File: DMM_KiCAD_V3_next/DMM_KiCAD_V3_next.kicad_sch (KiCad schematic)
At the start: 69 parts, among them J1 Conn_01x07_Pin, J10 ANALOG, J11 I_Input, J12 Conn_01x02_Pin, J13 DIGITAL1, J14 Barrel_Jack, J15 Barrel_Jack, J2 MicoSD, J3 Conn_01x07_Pin, J31 Conn_01x04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

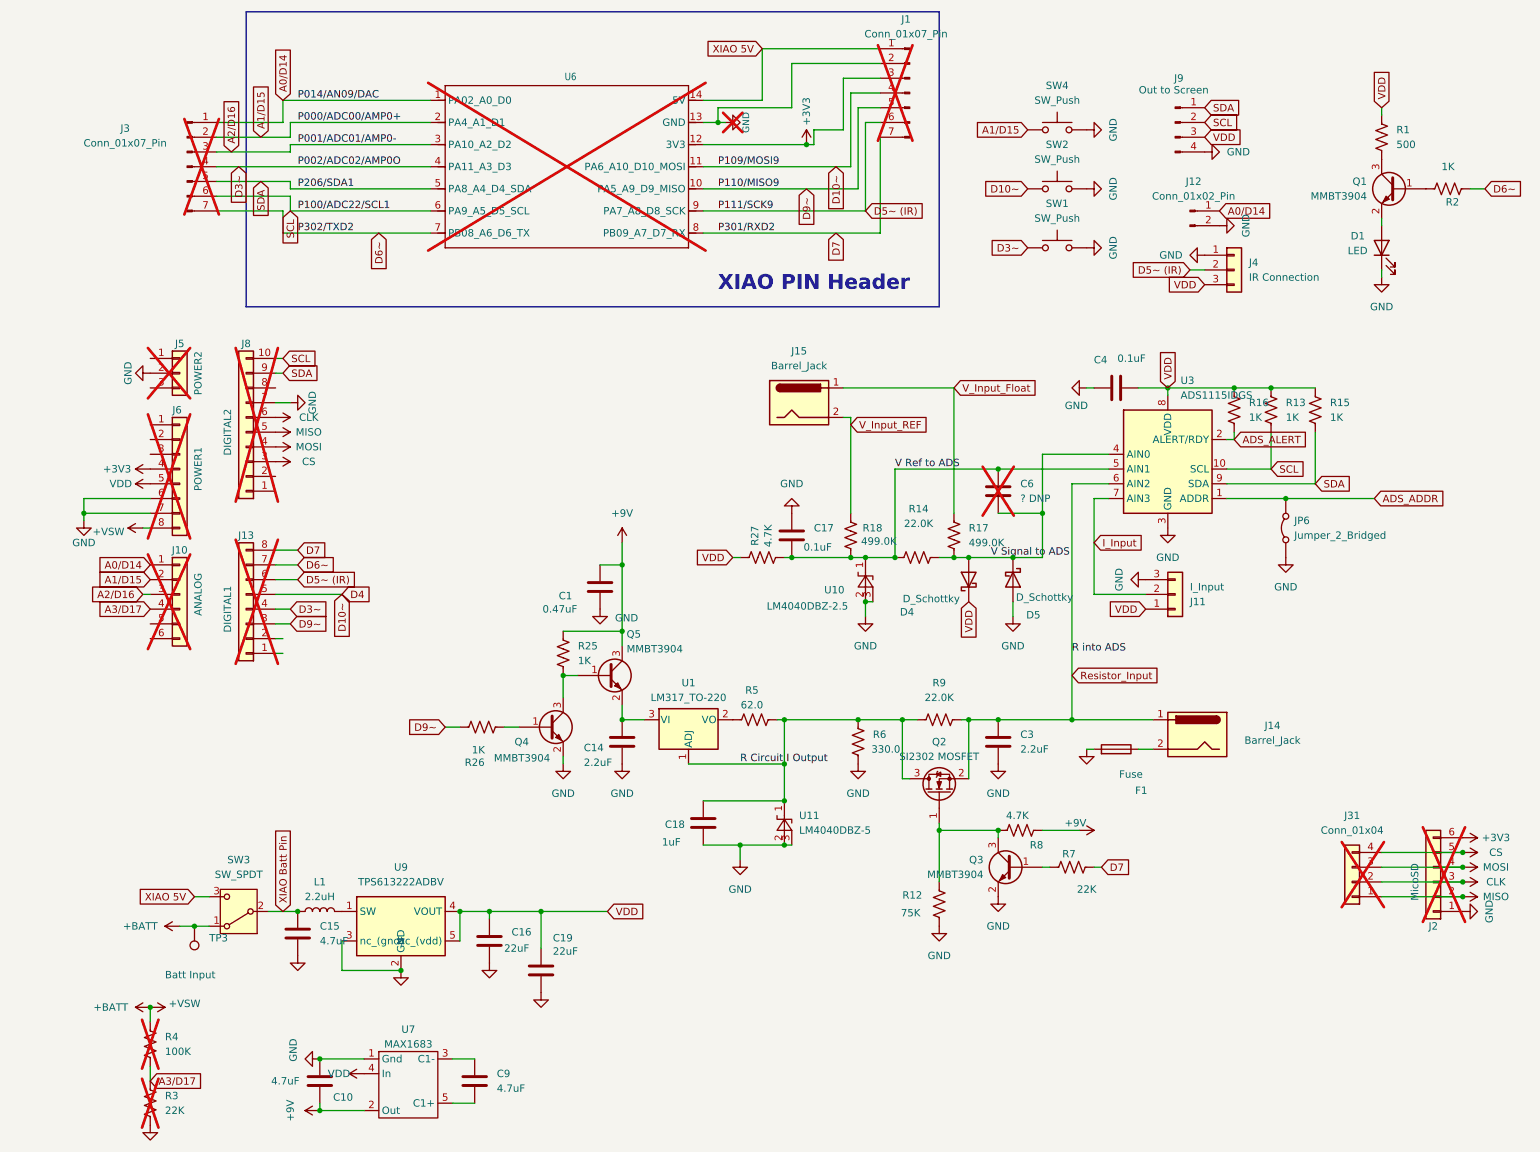
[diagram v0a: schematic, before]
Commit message: Working on a Giga-COmpatible DMM code.
Also working on adding level shifting to the next PCB design.
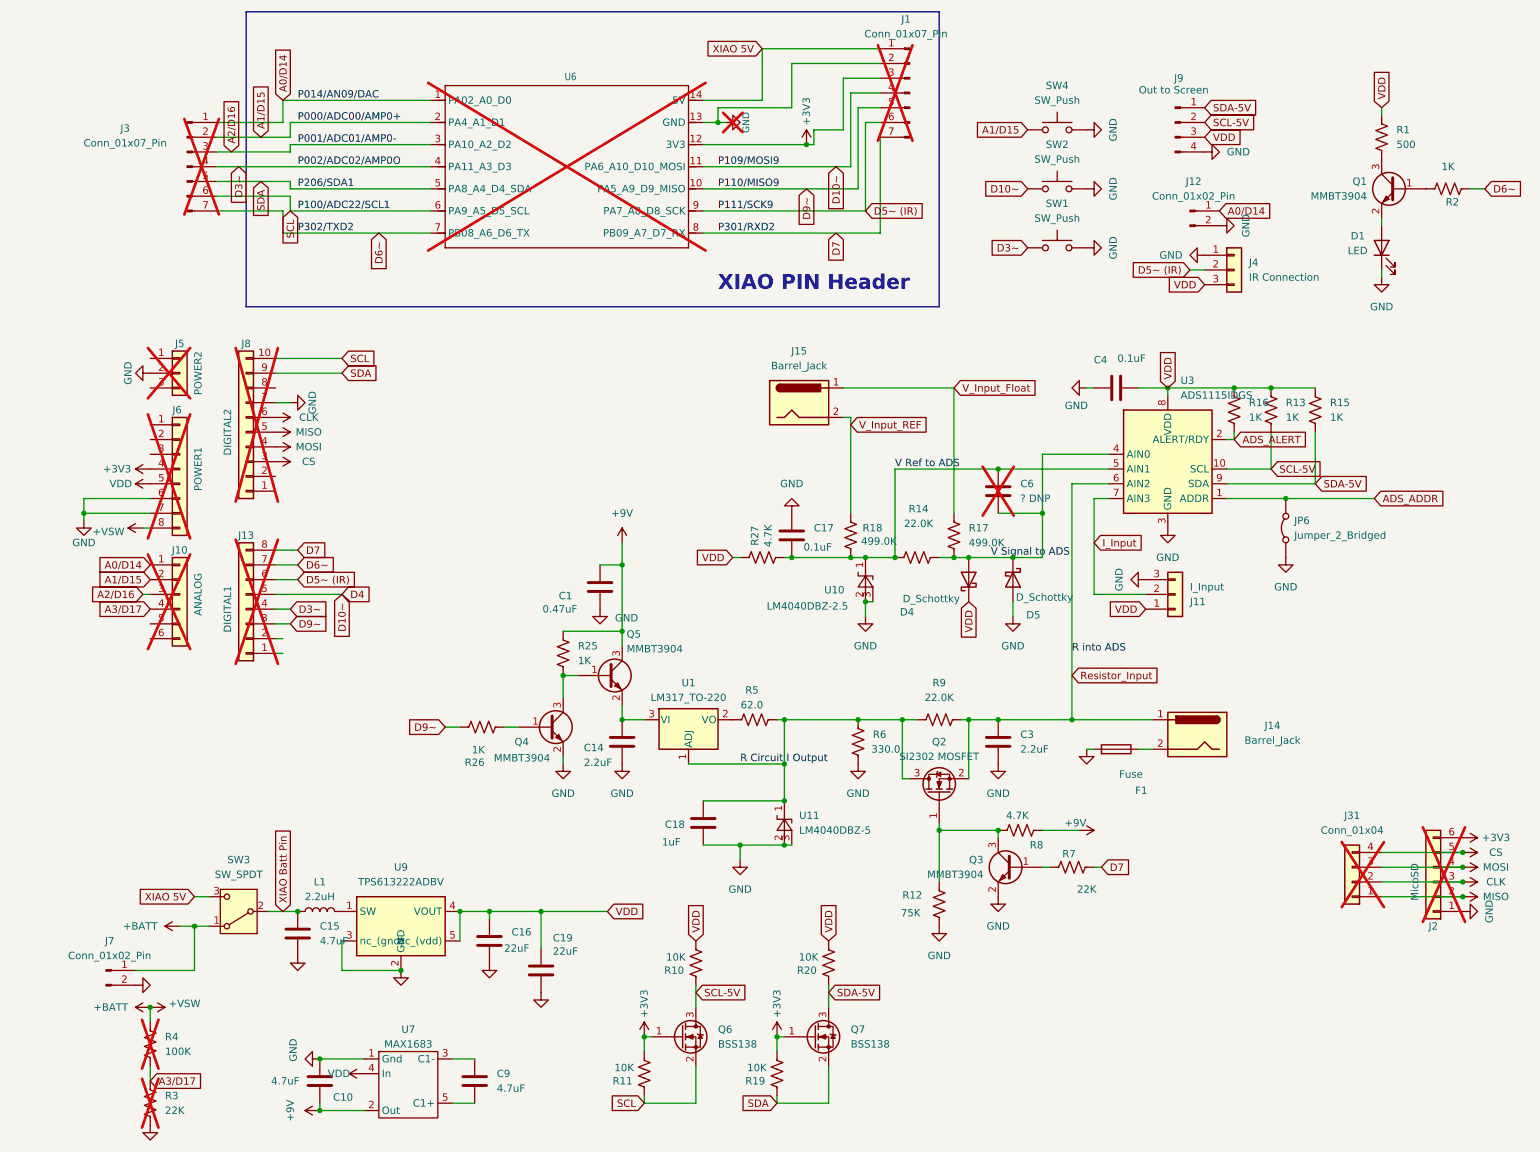
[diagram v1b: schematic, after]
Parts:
- removed TP3: Batt Input, Connector_PinHeader_2.54mm:PinHeader_1x01_P2.54mm_Vertical, symbol Connector:TestPoint
- added J7: Conn_01x02_Pin, Connector_PinSocket_2.54mm:PinSocket_1x02_P2.54mm_Vertical, symbol Connector:Conn_01x02_Pin
- added Q6, Q7: BSS138, Package_TO_SOT_SMD:SOT-23, symbol Transistor_FET:BSS138
- added R10, R11, R19, R20: 10K, Resistor_SMD:R_0805_2012Metric_Pad1.20x1.40mm_HandSolder, symbol Device:R_US
- F1: footprint Fuse:Fuseholder_Clip-5x20mm_Keystone_3512P_Inline_P23.62x7.27mm_D1.02x2.41x1.02x1.57mm_Horizontal -> Fuse:Fuse_1206_3216Metric_Pad1.42x1.75mm_HandSolder
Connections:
- net +3V3: now also Q6.1 (G), Q7.1 (G), R11.2, R19.2
- net +BATT: now also J7.1 (Pin_1)
- net GND: now also J7.2 (Pin_2)
- net SCL: now also Q6.2 (S), R11.1; no longer J9.2 (Pin_2), R13.1, U3.10 (SCL)
- net SDA: now also Q7.2 (S), R19.1; no longer J9.1 (Pin_1), R15.1, U3.9 (SDA)
- net VDD: now also R10.2, R20.2
- new net SCL-5V: J9.2 (Pin_2), Q6.3 (D), R10.1, R13.1, U3.10 (SCL)
- new net SDA-5V: J9.1 (Pin_1), Q7.3 (D), R15.1, R20.1, U3.9 (SDA)

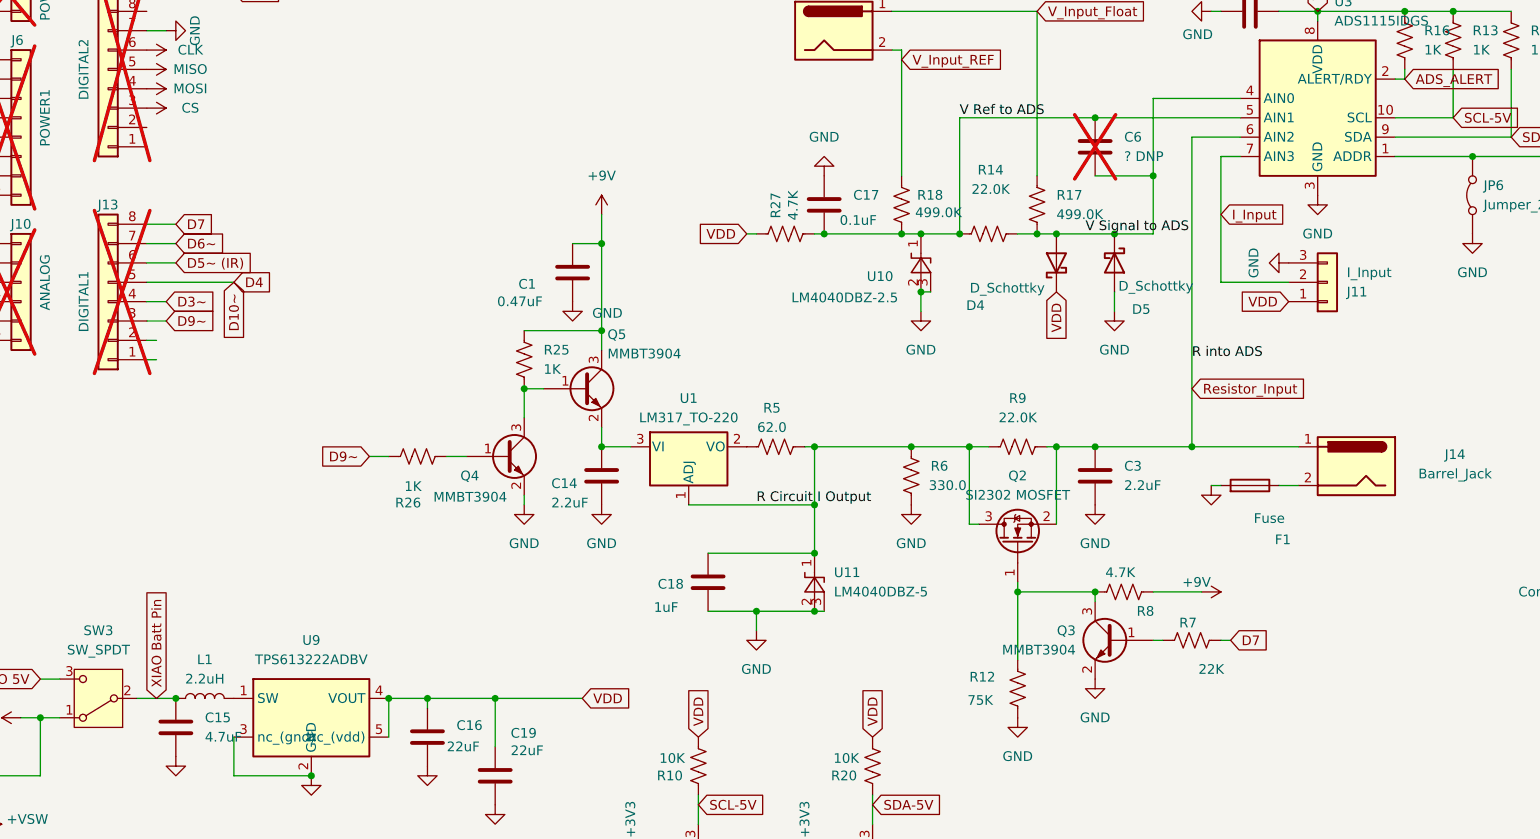
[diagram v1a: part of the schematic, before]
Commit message: PCB updates.
 Added the option for four-wire resistance measurements
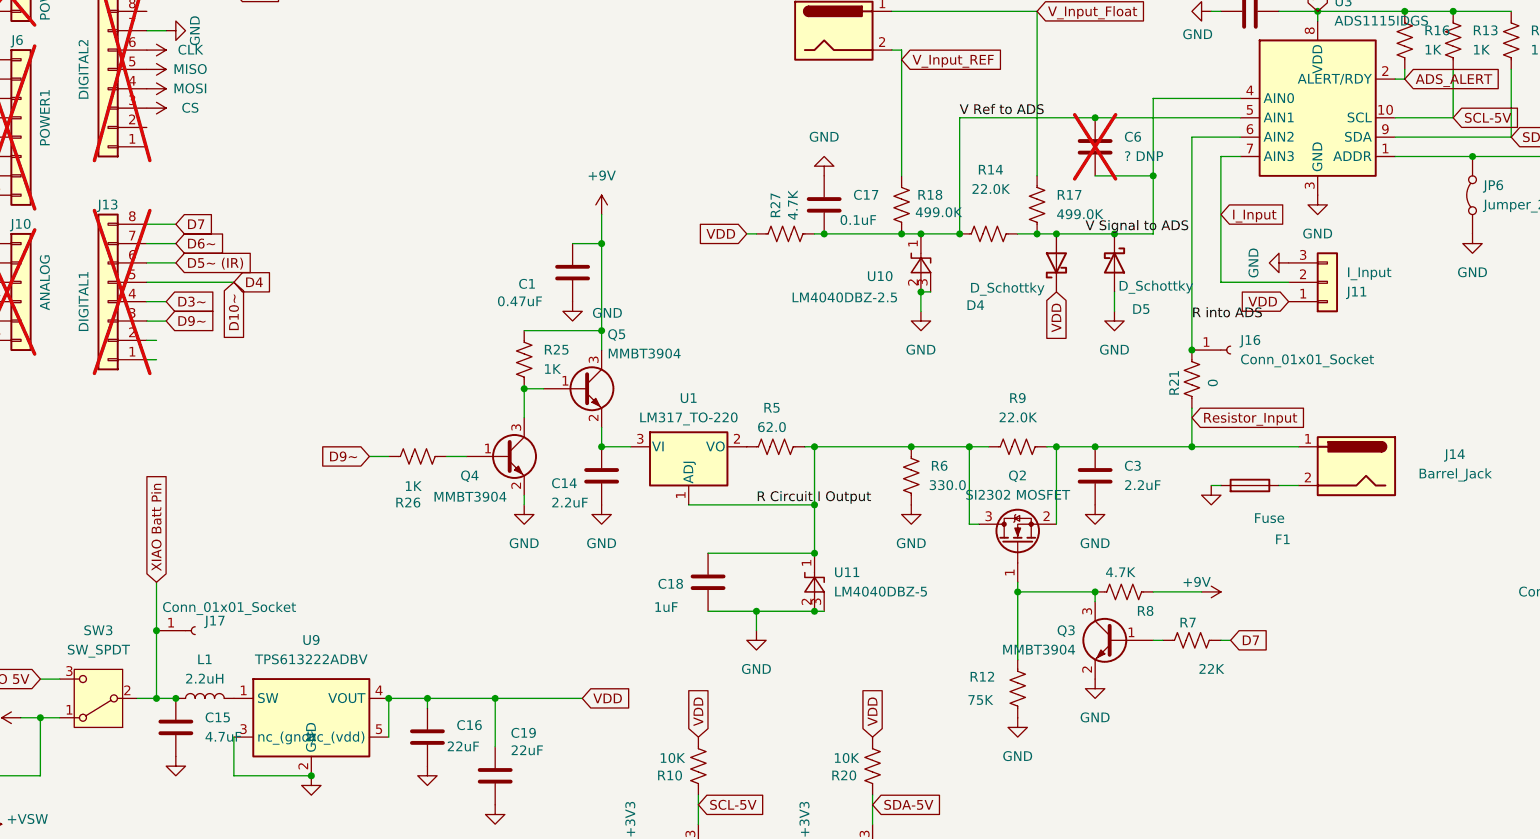
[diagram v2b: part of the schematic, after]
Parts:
- added J16, J17: Conn_01x01_Socket, Connector_PinSocket_2.54mm:PinSocket_1x01_P2.54mm_Vertical, symbol Connector:Conn_01x01_Socket
- added R21: 0, Resistor_SMD:R_0805_2012Metric_Pad1.20x1.40mm_HandSolder, symbol Device:R_US
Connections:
- net Resistor_Input: now also R21.2; no longer U3.6 (AIN2)
- net XIAO Batt Pin: now also J17.1 (Pin_1)
- new net R into ADS: J16.1 (Pin_1), R21.1, U3.6 (AIN2)

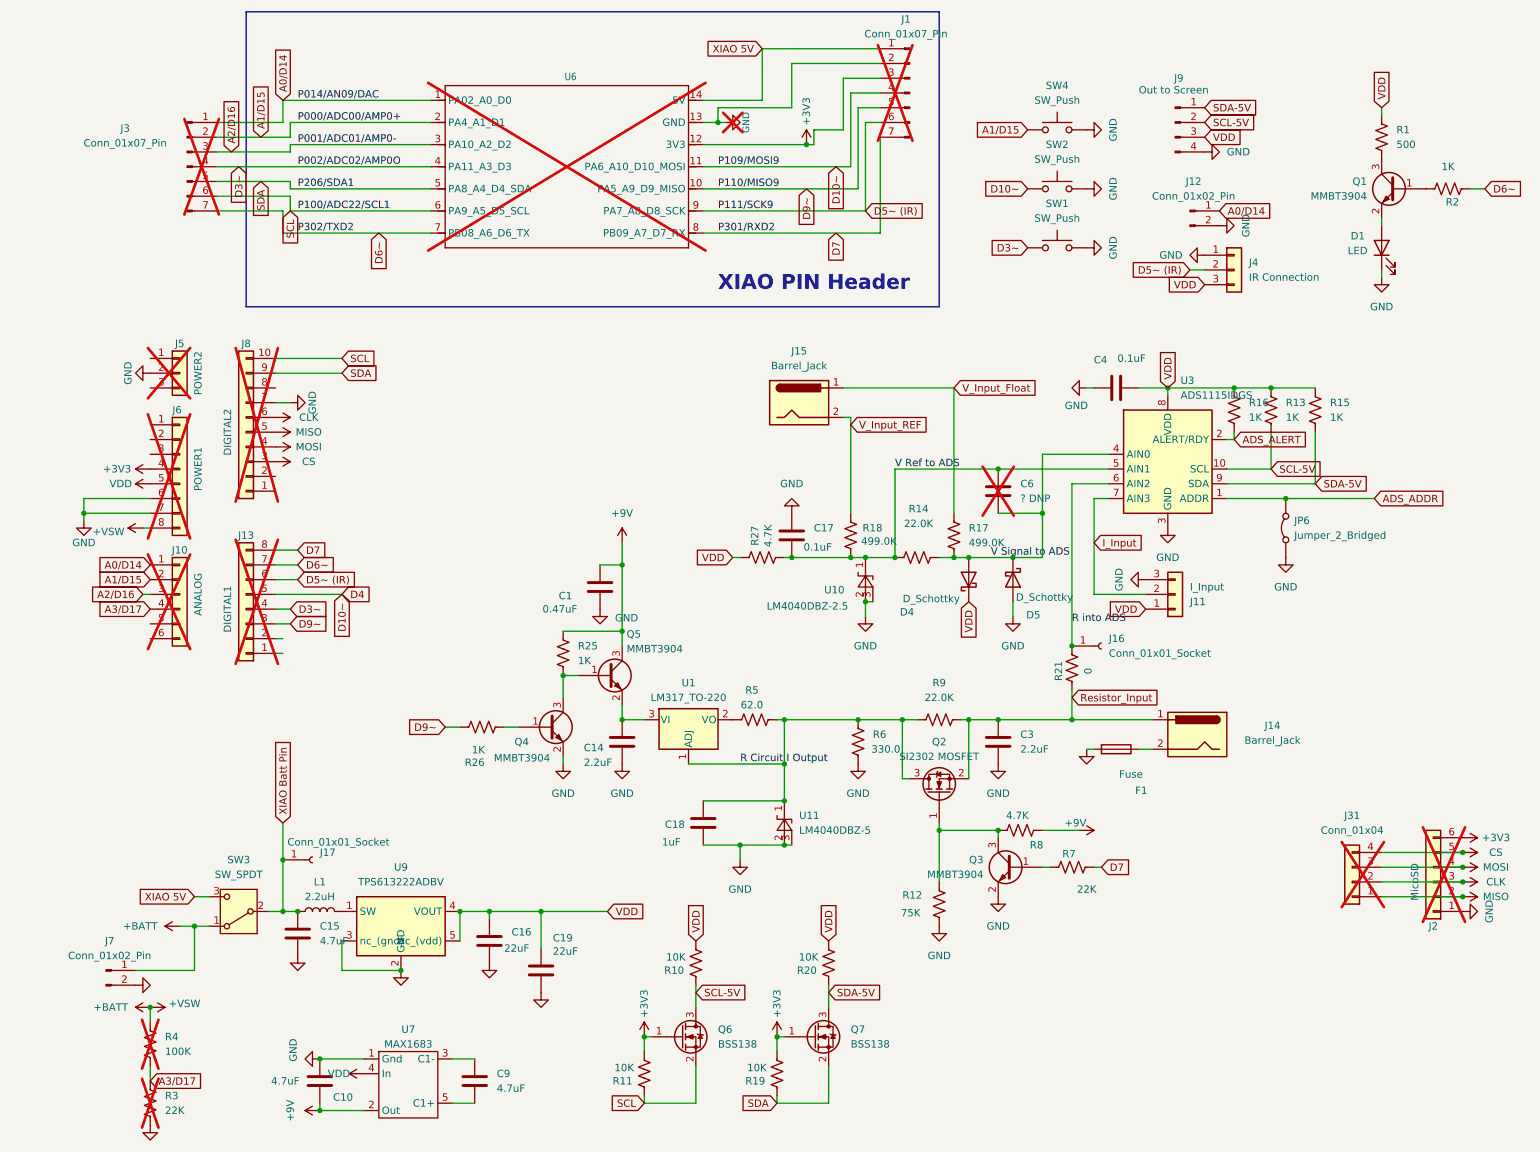
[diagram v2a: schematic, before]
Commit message: Added Touchscreen Buttons to the Giga Shield Version
Revised next PCB for power input options
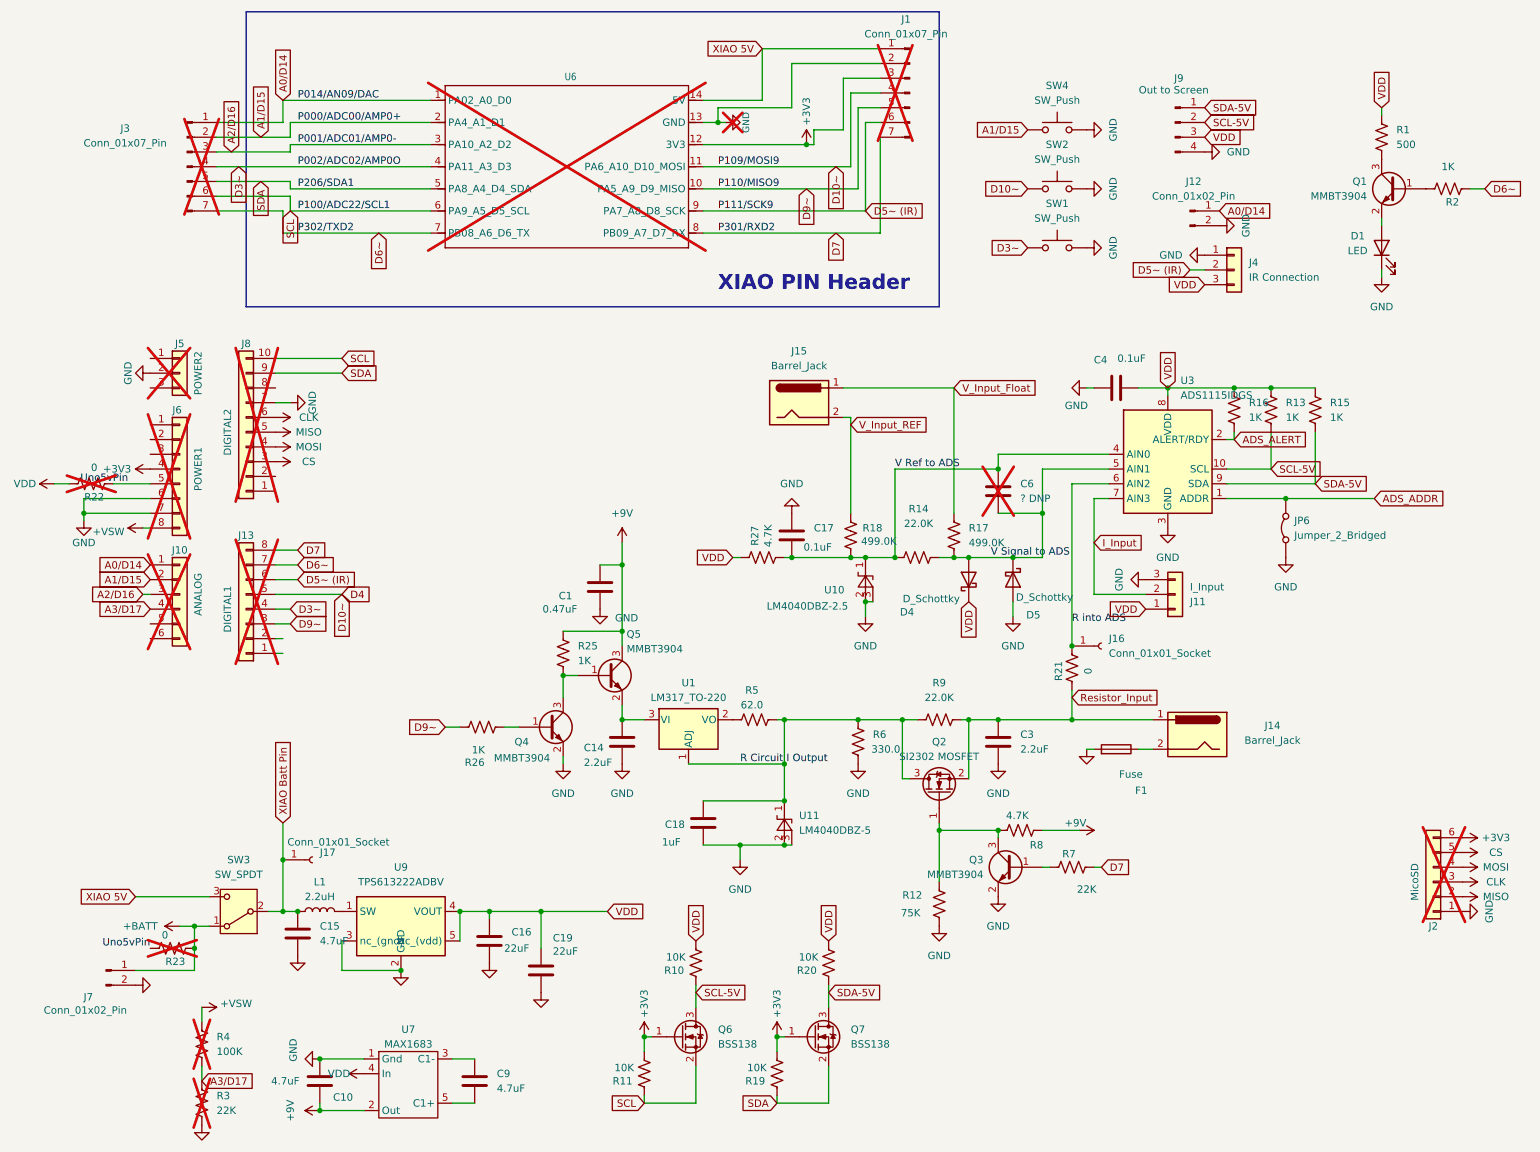
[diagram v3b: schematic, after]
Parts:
- removed J31: Conn_01x04, Connector_PinHeader_2.54mm:PinHeader_1x04_P2.54mm_Vertical, symbol Connector_Generic:Conn_01x04
- added R22, R23: 0, Resistor_SMD:R_0805_2012Metric_Pad1.20x1.40mm_HandSolder, symbol Device:R_US
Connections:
- net +BATT: now also R23.2; no longer J6.8 (Pin_8), R4.2
- net V Ref to ADS: now also U3.4 (AIN0); no longer U3.5 (AIN1)
- net V Signal to ADS: now also U3.5 (AIN1); no longer U3.4 (AIN0)
- net VDD: now also R22.1; no longer J6.5 (Pin_5)
- new net +VSW: J6.8 (Pin_8), R4.2
- new net Uno5vPin: J6.5 (Pin_5), R22.2, R23.1
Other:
- moved on the sheet: R3, R4
